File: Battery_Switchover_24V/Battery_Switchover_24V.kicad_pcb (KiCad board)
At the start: 2 copper layers, 9 parts, among them J8 USB_C_Receptacle_USB2.0_14P, U3 LPC11U14FBD48-201, U4 L5973D, U6 AMS1117-3.3

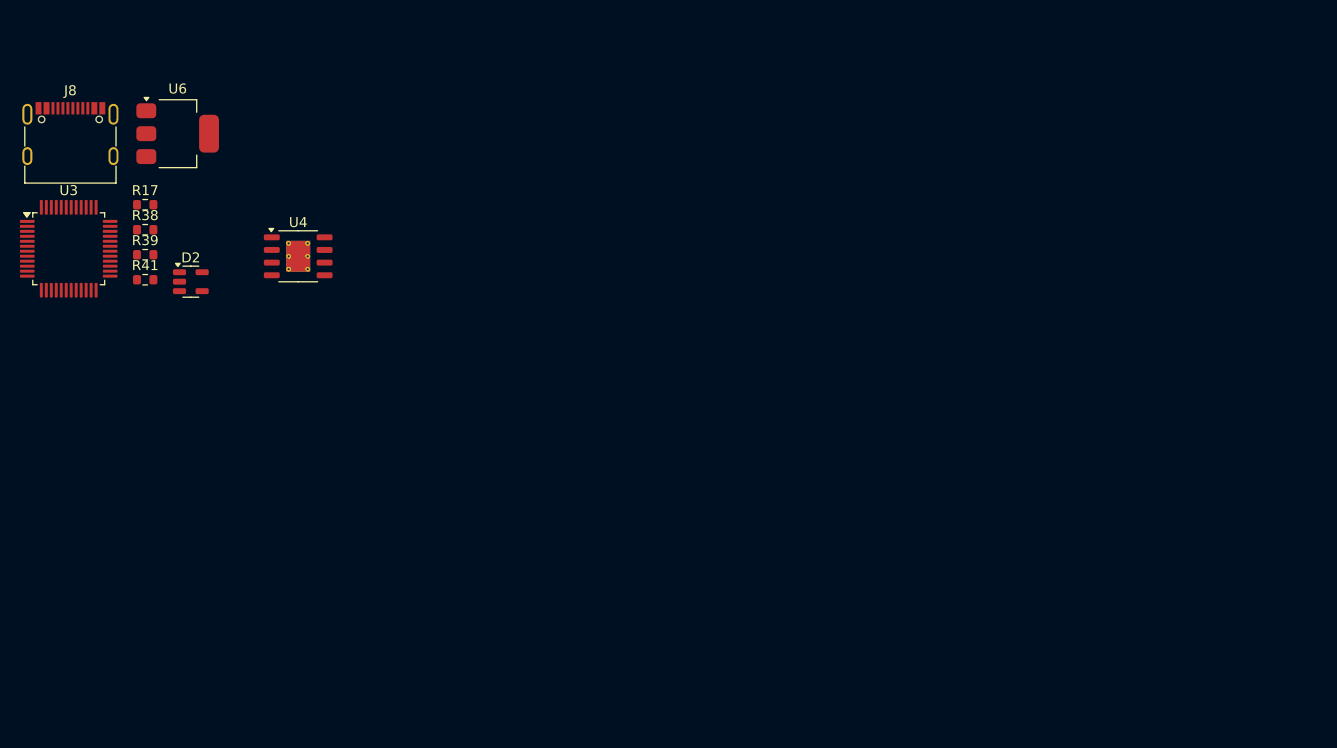
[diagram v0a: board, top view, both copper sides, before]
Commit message: Added Some Footprints
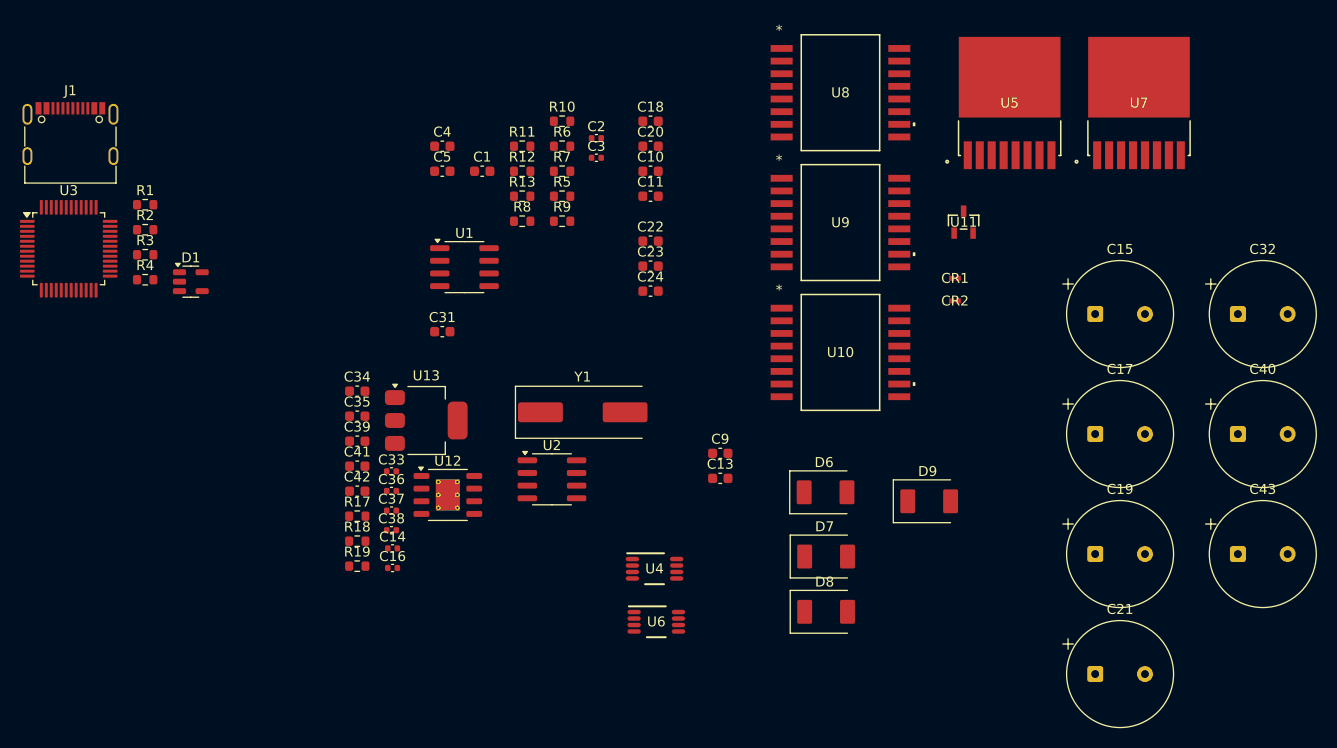
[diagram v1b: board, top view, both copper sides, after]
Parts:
- added C1: 1nF, Capacitor_SMD:C_0603_1608Metric, F.Cu at (123.9, 52.6)
- added C10: 1nF, Capacitor_SMD:C_0603_1608Metric, F.Cu at (140.8, 52.6)
- added C11: 1nF, Capacitor_SMD:C_0603_1608Metric, F.Cu at (140.8, 55.1)
- added C13: 100pF, Capacitor_SMD:C_0603_1608Metric, F.Cu at (147.8, 83.4)
- added C14: 1nF, Capacitor_SMD:C_0402_1005Metric, F.Cu at (114.9, 90.4)
- added C15: 330uF, Capacitor_THT:CP_Radial_Tantal_D10.5mm_P5.00mm, F.Cu at (185.5, 66.9)
- added C16: 1nF, Capacitor_SMD:C_0402_1005Metric, F.Cu at (114.9, 92.4)
- added C17: 330uF, Capacitor_THT:CP_Radial_Tantal_D10.5mm_P5.00mm, F.Cu at (185.5, 79.0)
- added C18: 10nF, Capacitor_SMD:C_0603_1608Metric, F.Cu at (140.8, 47.5)
- added C19: 330uF, Capacitor_THT:CP_Radial_Tantal_D10.5mm_P5.00mm, F.Cu at (185.5, 91.0)
- added C2: 18pF, Capacitor_SMD:C_0402_1005Metric, F.Cu at (135.4, 49.2)
- added C20: 100nF, Capacitor_SMD:C_0603_1608Metric, F.Cu at (140.8, 50.0)
- added C21: 330uF, Capacitor_THT:CP_Radial_Tantal_D10.5mm_P5.00mm, F.Cu at (185.5, 103.0)
- added C22: 100nF, Capacitor_SMD:C_0603_1608Metric, F.Cu at (140.8, 59.6)
- added C23: 100nF, Capacitor_SMD:C_0603_1608Metric, F.Cu at (140.8, 62.1)
- added C24: 100nF, Capacitor_SMD:C_0603_1608Metric, F.Cu at (140.8, 64.6)
- added C3: 18pF, Capacitor_SMD:C_0402_1005Metric, F.Cu at (135.4, 51.2)
- added C31: 100nF, Capacitor_SMD:C_0603_1608Metric, F.Cu at (119.9, 68.7)
- added C32: 330uF, Capacitor_THT:CP_Radial_Tantal_D10.5mm_P5.00mm, F.Cu at (199.8, 66.9)
- added C33: 1nF, Capacitor_SMD:C_0402_1005Metric, F.Cu at (114.8, 82.7)
- added C34: 10nF, Capacitor_SMD:C_0603_1608Metric, F.Cu at (111.4, 74.6)
- added C35: 100nF, Capacitor_SMD:C_0603_1608Metric, F.Cu at (111.4, 77.2)
- added C36: 1nF, Capacitor_SMD:C_0402_1005Metric, F.Cu at (114.8, 84.7)
- added C37: 22nF, Capacitor_SMD:C_0402_1005Metric, F.Cu at (114.8, 86.6)
- added C38: 220pF, Capacitor_SMD:C_0402_1005Metric, F.Cu at (114.8, 88.6)
- added C39: 100nF, Capacitor_SMD:C_0603_1608Metric, F.Cu at (111.4, 79.7)
- added C4: 100nF, Capacitor_SMD:C_0603_1608Metric, F.Cu at (119.9, 50.0)
- added C40: 330uF, Capacitor_THT:CP_Radial_Tantal_D10.5mm_P5.00mm, F.Cu at (199.8, 79.0)
- added C41: 100nF, Capacitor_SMD:C_0603_1608Metric, F.Cu at (111.4, 82.2)
- added C42: 1uF, Capacitor_SMD:C_0603_1608Metric, F.Cu at (111.4, 84.7)
- added C43: 330uF, Capacitor_THT:CP_Radial_Tantal_D10.5mm_P5.00mm, F.Cu at (199.8, 91.0)
- added C5: 100nF, Capacitor_SMD:C_0603_1608Metric, F.Cu at (119.9, 52.6)
- added C9: 100pF, Capacitor_SMD:C_0603_1608Metric, F.Cu at (147.8, 80.9)
- added CR1: PESD5V0S1BL, footprints:SOD882_NXP, F.Cu at (171.4, 63.3)
- added CR2: PESD5V0S1BL, footprints:SOD882_NXP, F.Cu at (171.4, 65.6)
- added D6: P6SMBJ26A, footprints:P26_DO-214AA_SMB, F.Cu at (156.2, 84.8)
- added D7: P6SMBJ26A, footprints:P26_DO-214AA_SMB, F.Cu at (156.3, 91.2)
- added D8: P6SMBJ26A, footprints:P26_DO-214AA_SMB, F.Cu at (156.3, 96.8)
- added D9: P6SMBJ26A, footprints:P26_DO-214AA_SMB, F.Cu at (166.7, 85.7)
- added R10: 500, Resistor_SMD:R_0603_1608Metric, F.Cu at (131.9, 47.5)
- added R11: 470R, Resistor_SMD:R_0603_1608Metric, F.Cu at (127.9, 50.0)
- added R12: 470R, Resistor_SMD:R_0603_1608Metric, F.Cu at (127.9, 52.6)
- added R13: 470R, Resistor_SMD:R_0603_1608Metric, F.Cu at (127.9, 55.1)
- added R17: 4.7K, Resistor_SMD:R_0603_1608Metric, F.Cu at (111.4, 87.2)
- added R18: 7.5K, Resistor_SMD:R_0603_1608Metric, F.Cu at (111.4, 89.7)
- added R19: 2.5K, Resistor_SMD:R_0603_1608Metric, F.Cu at (111.4, 92.2)
- added R5: 10K, Resistor_SMD:R_0603_1608Metric, F.Cu at (131.9, 55.1)
- added R6: 92.4K, Resistor_SMD:R_0603_1608Metric, F.Cu at (131.9, 50.0)
- added R7: 6.6K, Resistor_SMD:R_0603_1608Metric, F.Cu at (131.9, 52.6)
- added R8: 92.4K, Resistor_SMD:R_0603_1608Metric, F.Cu at (127.9, 57.6)
- added R9: 6.6K, Resistor_SMD:R_0603_1608Metric, F.Cu at (131.9, 57.6)
- added U1: OPA2197xD, Package_SO:SOIC-8_3.9x4.9mm_P1.27mm, F.Cu at (122.1, 62.2)
- added U10: ACS37002LMABTR-066B5, footprints:SOICW16_MC_ALM, F.Cu at (159.9, 70.8)
- added U11: LM60CIM3, footprints:MF03A, F.Cu at (172.3, 57.7)
- added U12: L5973D, Package_SO:HSOP-8-1EP_3.9x4.9mm_P1.27mm_EP2.41x3.1mm_ThermalVias, F.Cu at (120.5, 85.1)
- added U13: AMS1117-3.3, Package_TO_SOT_SMD:SOT-223-3_TabPin2, F.Cu at (118.3, 77.6)
- added U2: OPA2197xD, Package_SO:SOIC-8_3.9x4.9mm_P1.27mm, F.Cu at (130.9, 83.5)
- added U5: FDBL86066-F085, footprints:H-PSOF8L_ONS, F.Cu at (176.9, 45.7)
- added U7: FDBL86066-F085, footprints:H-PSOF8L_ONS, F.Cu at (189.9, 45.7)
- added U8: ACS37002LMABTR-066B5, footprints:SOICW16_MC_ALM, F.Cu at (159.9, 44.7)
- added U9: ACS37002LMABTR-066B5, footprints:SOICW16_MC_ALM, F.Cu at (159.9, 57.7)
- added Y1: 12.000MHz, Crystal:Crystal_SMD_HC49-SD, F.Cu at (134.0, 76.8)
- U4: value L5973D -> LM74610QDGKRQ1; footprint Package_SO:HSOP-8-1EP_3.9x4.9mm_P1.27mm_EP2.41x3.1mm_ThermalVias -> footprints:DGK0008A_N
- U6: value AMS1117-3.3 -> LM74610QDGKRQ1; footprint Package_TO_SOT_SMD:SOT-223-3_TabPin2 -> footprints:DGK0008A_N
- moved U6 68.6 mm to (141.4, 97.8)
- moved U4 47.6 mm to (141.2, 92.5)
- renumbered D2 to D1, J8 to J1, R17 to R1, R38 to R2, R39 to R3, R41 to R4
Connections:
- D1 pad 1: Net-(D2-K-Pad1) -> +5V
- J1 pad A4: Net-(D2-K-Pad1) -> +5V
- J1 pad A9: Net-(D2-K-Pad1) -> +5V
- J1 pad B4: Net-(D2-K-Pad1) -> +5V
- J1 pad B9: Net-(D2-K-Pad1) -> +5V
- U3 pad 13: unconnected-(U3-PIO1_20-Pad13) -> Battery_Status
- U3 pad 15: unconnected-(U3-PIO0_4-Pad15) -> SCL
- U3 pad 16: unconnected-(U3-PIO0_5-Pad16) -> SDA
- U3 pad 2: unconnected-(U3-PIO1_19-Pad2) -> Main_Voltage
- U3 pad 26: unconnected-(U3-PIO1_21-Pad26) -> Fan_Status
- U3 pad 29: unconnected-(U3-PIO0_10-Pad29) -> V_temp
- U3 pad 32: unconnected-(U3-PIO0_11-Pad32) -> ADC_In
- U3 pad 33: unconnected-(U3-PIO0_12-Pad33) -> ADC_Batt
- U3 pad 42: unconnected-(U3-PIO0_23-Pad42) -> Fan_Control
- U4 pad 2: unconnected-(U4-SYNC-Pad2) -> Net-(U4-GATE_DRIVE)
- U4 pad 3: GND -> unconnected-(U4-NC-Pad3)
- U4 pad 4: Net-(U4-COMP) -> Vin
- U4 pad 5: Net-(U4-FB) -> unconnected-(U4-NC-Pad5)
- U4 pad 6: unconnected-(U4-VREF-Pad6) -> Net-(U4-GATE_DRIVE)
- U4 pad 7: GND -> Net-(U4-VCAPH)
- U6 pad 1: GND -> Net-(U6-VCAPL)
- U6 pad 2: +3.3V -> Net-(U6-GATE_DRIVE)
- U6 pad 3: +5V -> unconnected-(U6-NC-Pad3)

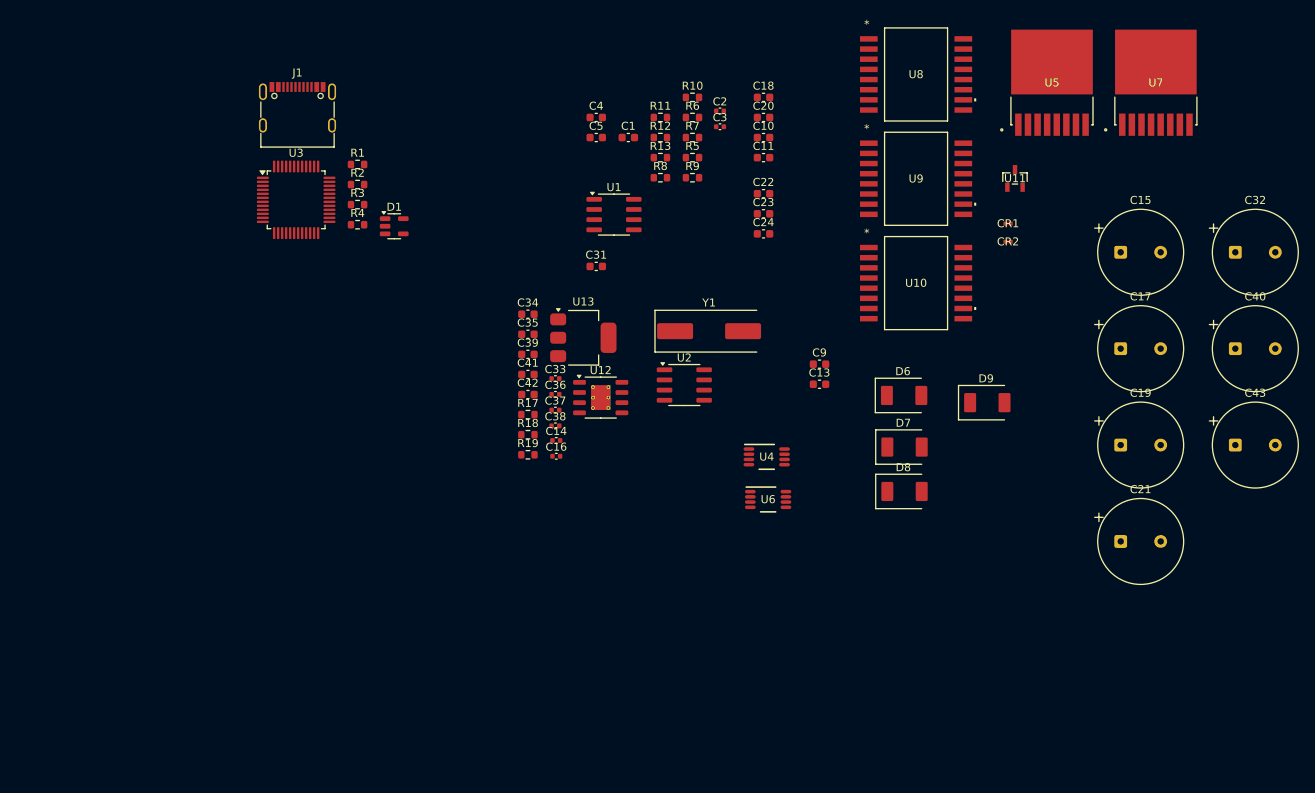
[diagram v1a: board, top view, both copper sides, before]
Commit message: Added common mode chokes for input and output of the load fixed the corrupted board
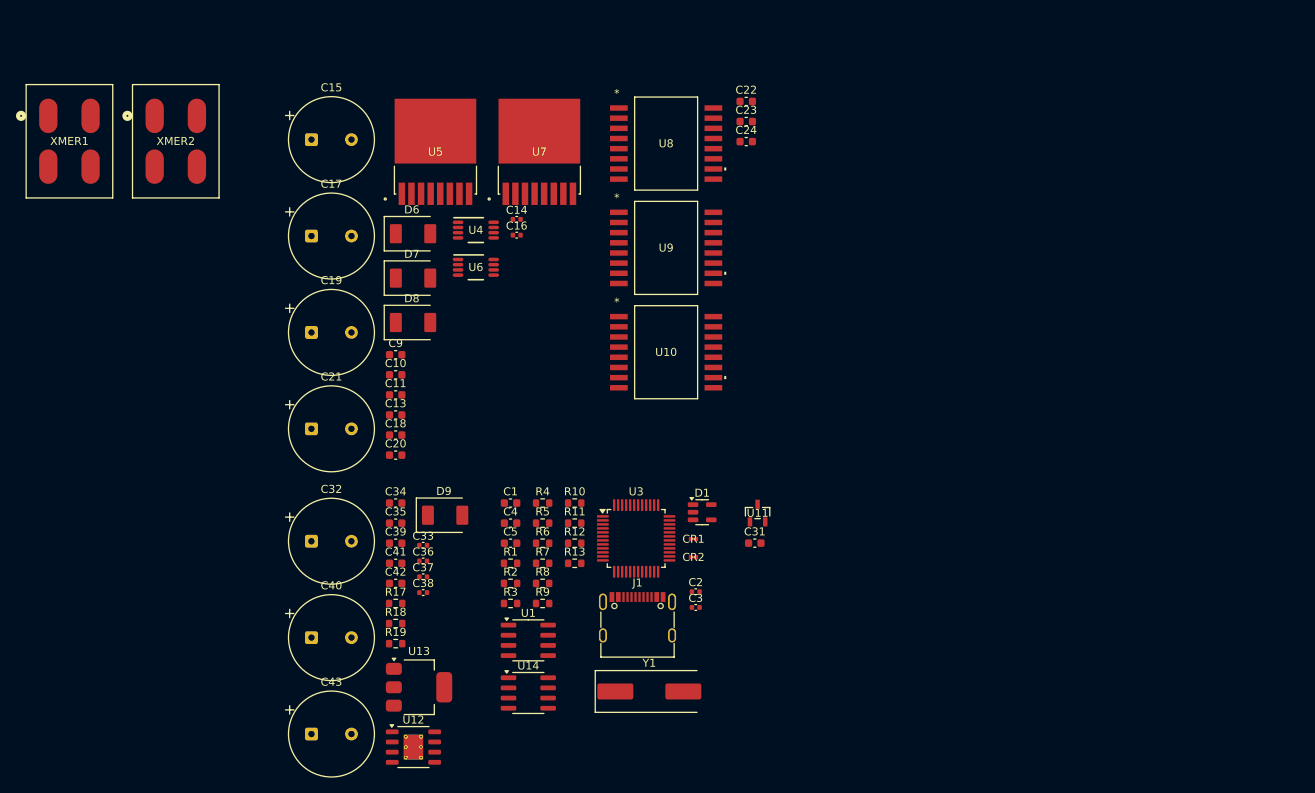
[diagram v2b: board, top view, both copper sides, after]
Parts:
- removed U2: OPA2197xD, Package_SO:SOIC-8_3.9x4.9mm_P1.27mm
- added U14: OPA2197xD, Package_SO:SOIC-8_3.9x4.9mm_P1.27mm, F.Cu at (111.4, 122.0)
- added XMER1: CM5441Z101B-10, footprints:CM5441Z101B-10_LRD, F.Cu at (51.4, 49.9)
- added XMER2: CM5441Z101B-10, footprints:CM5441Z101B-10_LRD, F.Cu at (64.7, 49.9)
- moved C32 121.0 mm to (84.3, 103.0)
- moved C40 121.0 mm to (84.3, 115.1)
- moved C43 121.0 mm to (84.3, 127.1)
- moved C15 102.1 mm to (84.3, 52.8)
- moved C17 102.1 mm to (84.3, 64.9)
- moved C19 102.1 mm to (84.3, 76.9)
- moved C21 102.1 mm to (84.3, 89.0)
- moved U5 77.5 mm to (99.8, 54.3)
- moved U7 77.5 mm to (112.8, 54.3)
- moved J1 76.6 mm to (125.1, 113.7)
- moved D9 69.2 mm to (98.9, 99.8)
- moved D7 65.0 mm to (94.9, 70.1)
- moved D8 65.0 mm to (94.9, 75.7)
- moved D6 64.6 mm to (94.9, 64.6)
- moved C20 62.4 mm to (94.8, 92.3)
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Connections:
- C14 pad 1: Vbatt -> Vsupply
- C15 pad 1: Vbatt -> Vsupply
- C16 pad 1: Vbatt -> Vsupply
- C17 pad 1: Vbatt -> Vsupply
- C18 pad 1: Vbatt -> Vsupply
- C19 pad 1: Vbatt -> Vsupply
- C20 pad 1: Vbatt -> Vsupply
- C21 pad 1: Vbatt -> Vsupply
- C32 pad 1: Vbatt -> Vsupply
- C33 pad 2: Vbatt -> Vsupply
- C34 pad 2: Vbatt -> Vsupply
- C35 pad 2: Vbatt -> Vsupply
- C36 pad 2: Vbatt -> Vsupply
- C9 pad 1: Vin -> Net-(D6-A2)
- CR1 pad 2: Net-(U1A-+) -> Net-(U14A-+)
- CR2 pad 2: Net-(U2A-+) -> Net-(U1B-+)
- D6 pad 2: Vin -> Net-(D6-A2)
- D8 pad 2: Vbatt -> Vsupply
- D9 pad 2: Vbatt -> Vsupply
- R6 pad 1: Net-(U1A-+) -> Net-(U14A-+)
- R7 pad 2: Net-(U1A-+) -> Net-(U14A-+)
- R8 pad 1: Net-(U2A-+) -> Net-(U1B-+)
- R9 pad 2: Net-(U2A-+) -> Net-(U1B-+)
- U1 pad 1: ADC_Batt -> (no net)
- U1 pad 2: ADC_Batt -> (no net)
- U1 pad 3: Net-(U1A-+) -> (no net)
- U1 pad 4: (no net) -> GND
- U1 pad 5: (no net) -> Net-(U1B-+)
- U1 pad 6: (no net) -> ADC_In
- U1 pad 7: (no net) -> ADC_In
- U1 pad 8: (no net) -> +5V
- U12 pad 8: Vbatt -> Vsupply
- U4 pad 4: Vin -> Net-(D6-A2)
- U5 pad 2: Vin -> Net-(D6-A2)
- U5 pad 3: Vin -> Net-(D6-A2)
- U5 pad 4: Vin -> Net-(D6-A2)
- U5 pad 5: Vin -> Net-(D6-A2)
- U5 pad 6: Vin -> Net-(D6-A2)
- U5 pad 7: Vin -> Net-(D6-A2)
- U5 pad 8: Vin -> Net-(D6-A2)
